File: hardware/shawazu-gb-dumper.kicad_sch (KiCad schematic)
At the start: 15 parts, among them J1 GB_CART, SW1 VSEL, U1 BOB-12009, U2 BOB-12009, U3 BOB-12009, U4 BOB-12009, U5 BOB-12009, U6 BOB-12009, U7 BOB-12009, U8 Pico

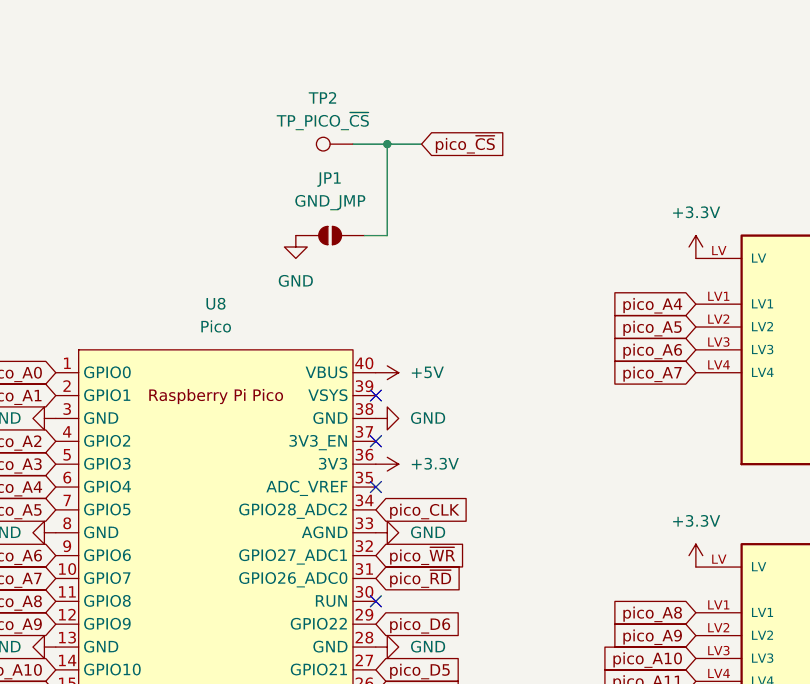
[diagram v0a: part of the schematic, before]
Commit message: switched TP nCS with CLK
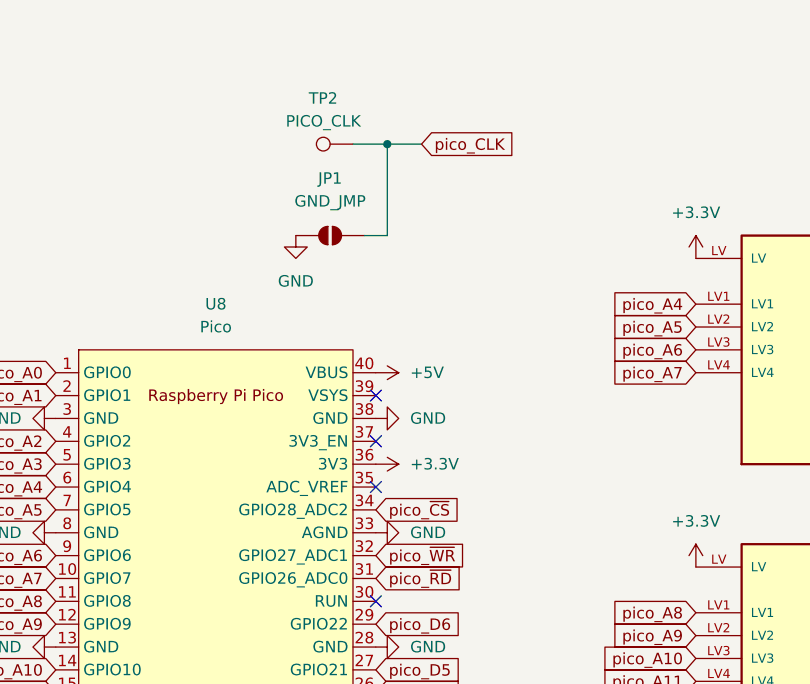
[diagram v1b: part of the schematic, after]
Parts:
- TP2: value TP_PICO_~{CS} -> PICO_CLK
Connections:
- net pico_CLK: now also JP1.2 (B), TP2.1; no longer U8.34 (GPIO28_ADC2)
- net pico_~{CS}: now also U8.34 (GPIO28_ADC2); no longer JP1.2 (B), TP2.1
